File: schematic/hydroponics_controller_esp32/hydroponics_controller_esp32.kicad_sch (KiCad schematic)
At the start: 26 parts, among them J1 12v -, J10 RJ45, J11 5v-16v in, J12 12v_4_Channel_Relay, J13 Conn_01x04_Pin, J14 Conn_01x04_Pin, J2 12v +, J3 RJ45, J4 Power Input, J5 Flow Meters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

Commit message: Created Schematic PDF
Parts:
- added U9: 0-5v, symbol Amazon_Modules:Pressure Sensor
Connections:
- net at U6. (Blk): now also U5. (Blk); no longer U2. (GND)
- net at U8. (Blk): now also U7. (Blk); no longer U6. (Blk)
- net at U5. (Blk): now also U7. (Blk); no longer U6. (Blk)
- net at J12.2 (GND): now also J2.5 (Pin_5); no longer J14.GND
- net at J12.3 (IN1): now also U3.6 (D32_GPIO32)
- net at J12.6 (IN4): now also U3.10 (D27_GPIO27)
- net at J13.3v3: now also J10.1 (3v3), J4.3V3
- net at U2. (GND): now also U5. (Blk)
- net at J8.8 (A1): now also U9.3 (Vout)
- new net: U2. (GND), U6. (Blk)
- new net: U6. (Blk), U8. (Blk)
- new net: J12.1 (VCC), J13.5v, J8.1 (VCC), U4. (SIG), U9.2 (Vcc)
- new net: J12.2 (GND), J14.GND, U9.1 (GND)
- new net: U2. (GND), U7. (Blk)
- new net: U2. (GND), U8. (Blk)
- now unconnected: J13.5v, U4. (SIG)
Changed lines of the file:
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@@
 	)
 	(junction
+		(at 115.57 77.47)
+		(diameter 0)
+		(color 0 0 0 0)
+	)
+	(junction
 		(at 95.25 151.13)
 		(diameter 0)
@@
 	)
 	(junction
+		(at 101.6 72.39)
+		(diameter 0)
+		(color 0 0 0 0)
+	)
+	(junction
 		(at 231.14 156.21)
 		(diameter 0)
@@
 	(wire
 		(pts
-			(xy 101.6 77.47) (xy 101.6 58.42)
+			(xy 101.6 77.47) (xy 101.6 72.39)
+		)
+		(stroke
+			(width 0)
+			(type default)
+		)
+	)
+	(wire
+		(pts
+			(xy 106.68 74.93) (xy 106.68 72.39)
 		)
 		(stroke
@@
 	(wire
 		(pts
+			(xy 115.57 77.47) (xy 115.57 55.88)
+		)
+		(stroke
+			(width 0)
+			(type default)
+		)
+	)
+	(wire
+		(pts
+			(xy 196.85 85.09) (xy 196.85 100.33)
+		)
+		(stroke
+			(width 0)
+			(type default)
+		)
+	)
+	(wire
+		(pts
 			(xy 50.8 97.79) (xy 25.4 97.79)
 		)
@@
 	(wire
 		(pts
+			(xy 189.23 74.93) (xy 106.68 74.93)
+		)
+		(stroke
+			(width 0)
+			(type default)
+		)
+	)
+	(wire
+		(pts
 			(xy 45.72 165.1) (xy 45.72 148.59)
 		)
@@
 	(wire
 		(pts
+			(xy 210.82 74.93) (xy 210.82 87.63)
+		)
+		(stroke
+			(width 0)
+			(type default)
+		)
+	)
+	(wire
+		(pts
 			(xy 43.18 179.07) (xy 22.86 179.07)
 		)
@@
 	(wire
 		(pts
+			(xy 101.6 72.39) (xy 101.6 58.42)
+		)
+		(stroke
+			(width 0)
+			(type default)
+		)
+	)
+	(wire
+		(pts
+			(xy 106.68 72.39) (xy 101.6 72.39)
+		)
+		(stroke
+			(width 0)
+			(type default)
+		)
+	)
+	(wire
+		(pts
 			(xy 220.98 153.67) (xy 220.98 156.21)
 		)
@@
 	(wire
 		(pts
+			(xy 138.43 96.52) (xy 138.43 100.33)
+		)
+		(stroke
+			(width 0)
+			(type default)
+		)
+	)
+	(wire
+		(pts
 			(xy 128.27 107.95) (xy 128.27 101.6)
 		)
@@
 	(wire
 		(pts
+			(xy 210.82 87.63) (xy 154.94 87.63)
+		)
+		(stroke
+			(width 0)
+			(type default)
+		)
+	)
+	(wire
+		(pts
 			(xy 220.98 143.51) (xy 220.98 146.05)
 		)
@@
 	(wire
 		(pts
+			(xy 154.94 77.47) (xy 115.57 77.47)
+		)
+		(stroke
+			(width 0)
+			(type default)
+		)
+	)
+	(wire
+		(pts
 			(xy 233.68 73.66) (xy 238.76 73.66)
 		)
@@
 	(wire
 		(pts
-			(xy 115.57 99.06) (xy 115.57 55.88)
+			(xy 115.57 99.06) (xy 115.57 77.47)
 		)
 		(stroke
@@
 	(wire
 		(pts
+			(xy 154.94 87.63) (xy 154.94 77.47)
+		)
+		(stroke
+			(width 0)
+			(type default)
+		)
+	)
+	(wire
+		(pts
 			(xy 80.01 33.02) (xy 116.84 33.02)
 		)
@@
 	(wire
 		(pts
+			(xy 204.47 74.93) (xy 210.82 74.93)
+		)
+		(stroke
+			(width 0)
+			(type default)
+		)
+	)
+	(wire
+		(pts
 			(xy 209.55 121.92) (xy 209.55 143.51)
 		)
@@
 	(wire
 		(pts
+			(xy 196.85 100.33) (xy 138.43 100.33)
+		)
+		(stroke
+			(width 0)
+			(type default)
+		)
+	)
+	(wire
+		(pts
 			(xy 40.64 113.03) (xy 50.8 113.03)
 		)
@@
 					(unit 1)
 				)
+			)
+		)
+	)
+	(symbol
+		(lib_id "Amazon_Modules:Pressure Sensor")
+		(at 196.85 72.39 0)
+		(unit 1)
+		(exclude_from_sim no)
+		(in_bom yes)
+		(on_board yes)
+		(dnp no)
+		(fields_autoplaced yes)
+		(property "Reference" "U9"
+			(at 196.85 58.42 0)
+			(effects
+				(font
+					(size 1.27 1.27)
+				)
+			)
+		)
+		(property "Value" "0-5v"
+			(at 196.85 60.96 0)
+			(effects
+				(font
+					(size 1.27 1.27)
+				)
+			)
+		)
+		(property "Footprint" ""
+			(at 184.15 81.28 0)
+			(effects
+				(font
+					(size 1.27 1.27)
+				)
+				(hide yes)
+			)
+		)
+		(property "Datasheet" "https://www.amazon.com/dp/B0CSWFWCVK?ref=fed_asin_title&th=1"
+			(at 196.85 57.15 0)
+			(effects
+				(font
+					(size 1.27 1.27)
+				)
+				(hide yes)
+			)
+		)
+		(property "Description" "Submersible Liquid Level Sensor"
+			(at 196.088 92.202 0)
+			(effects
+				(font
+					(size 1.27 1.27)
+				)
+				(hide yes)
+			)
+		)
+		(pin "3"
+		)
+		(pin "1"
+		)
+		(pin "2"
+		)
+		(instances
+			(project ""
+				(path "/0e72da9f-540e-48b3-a96e-9cdd4d439927"
+					(reference "U9")
+					(unit 1)
+				)

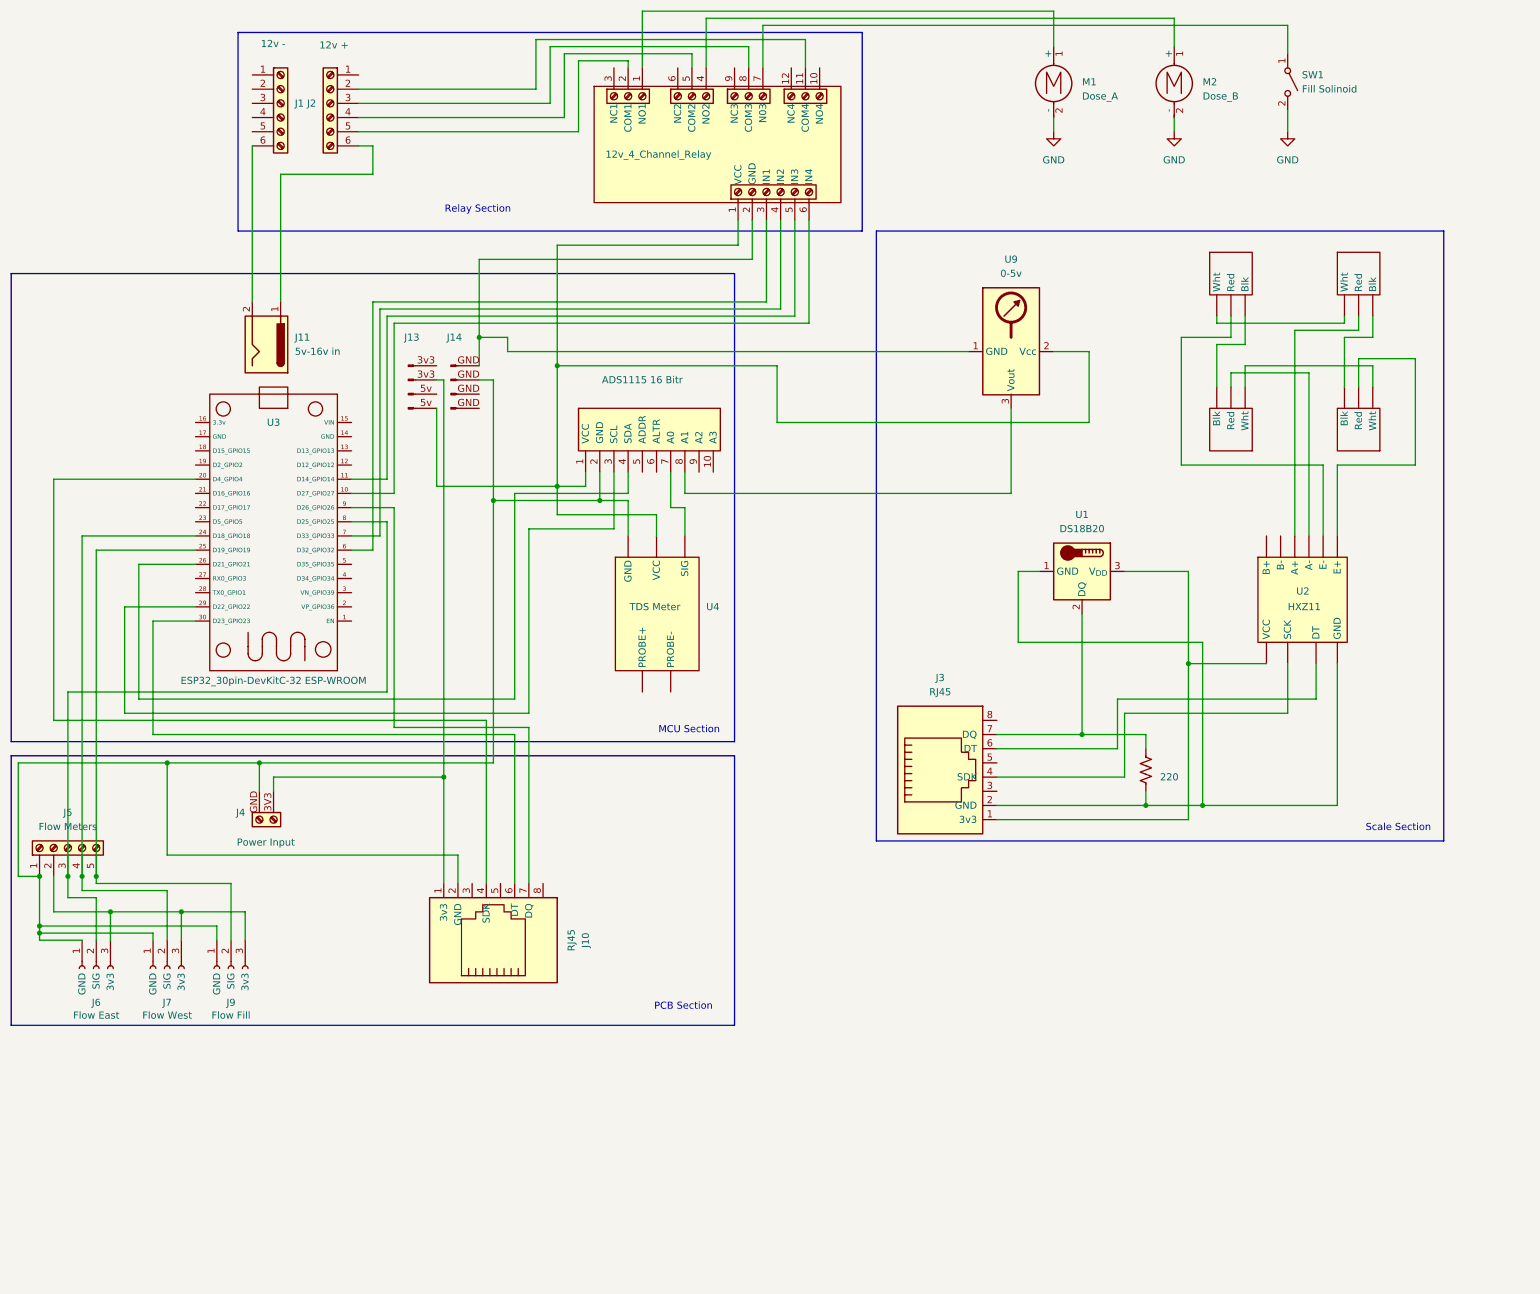
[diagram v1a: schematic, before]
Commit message: Hydroponics project architecture redesign
- Reorganized Home Assistant packages
- Added Node-RED workflow exports
- Added SQL schema
- Added engineering documentation
- Added project design documents
- Updated ESPHome controller
- Updated KiCad schematic
- Replaced nutrient mixing documentation
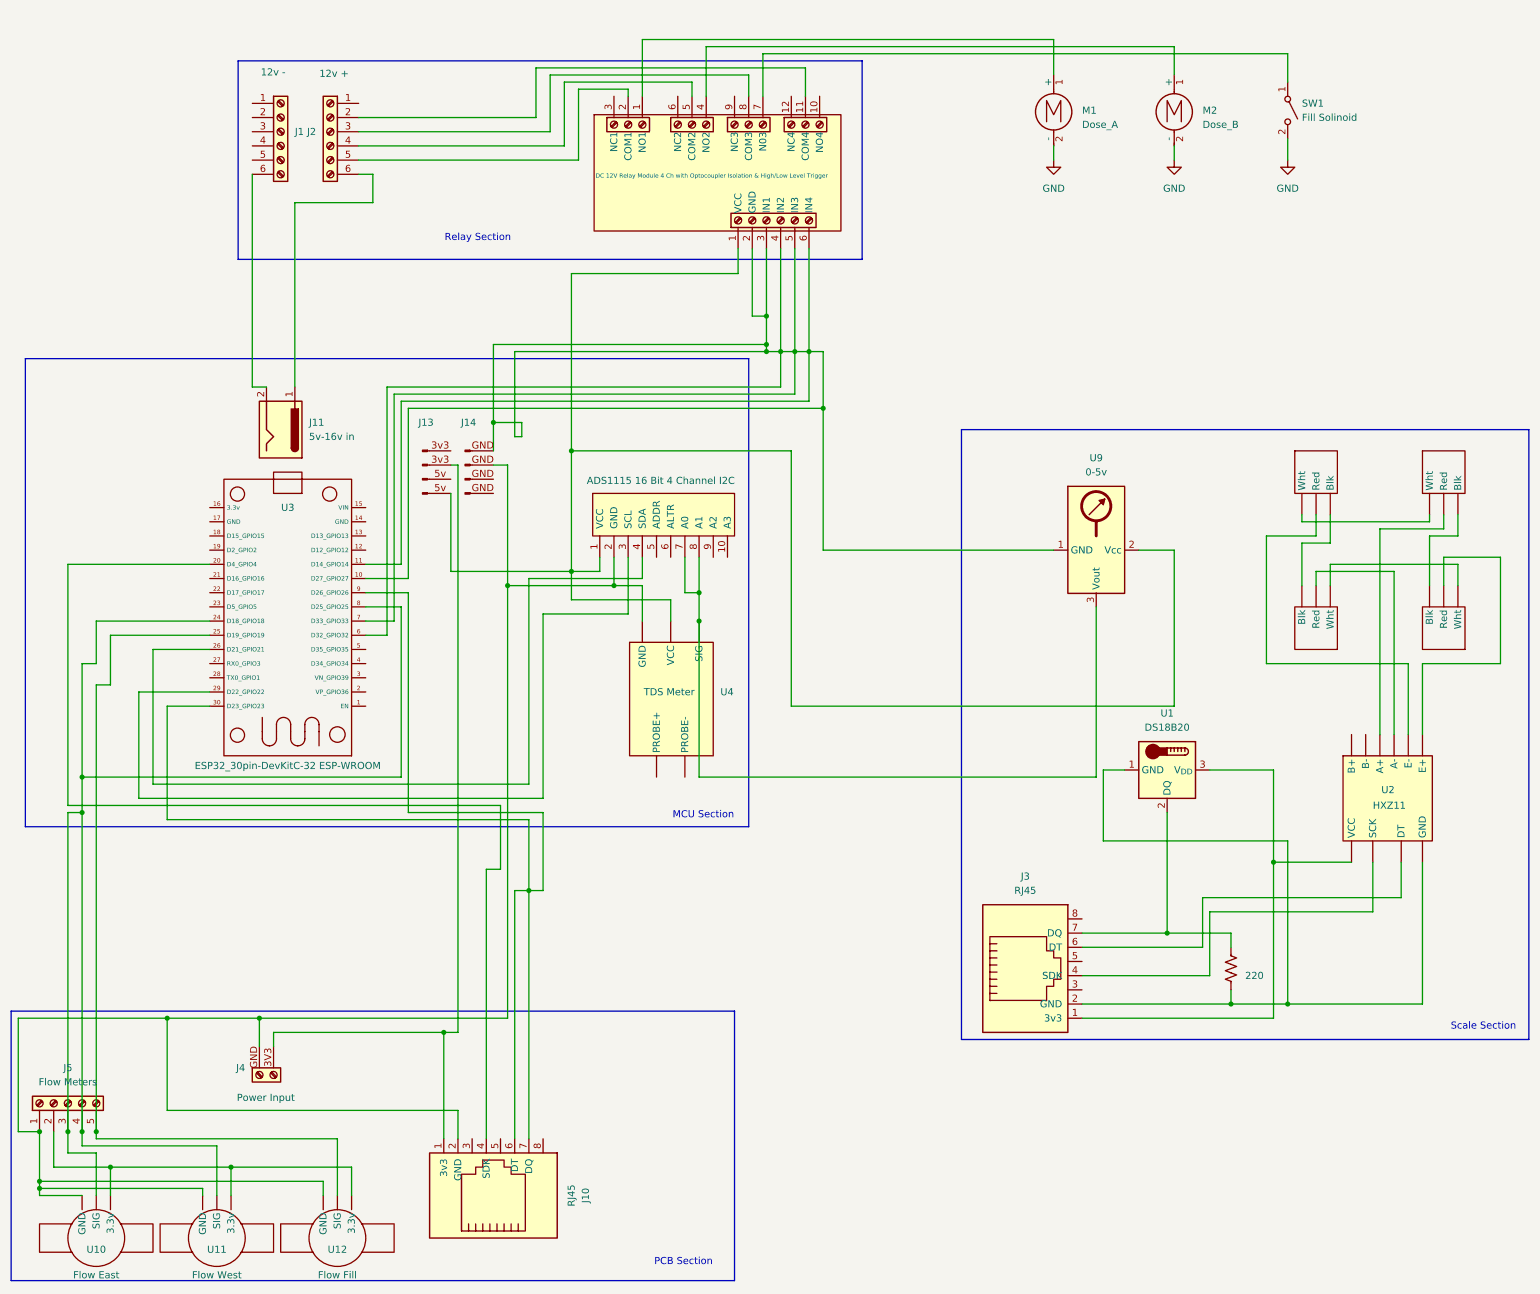
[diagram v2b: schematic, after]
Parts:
- removed J6: Flow East, symbol Connector:Conn_01x03_Socket
- removed J7: Flow West, symbol Connector:Conn_01x03_Socket
- removed J9: Flow Fill, symbol Connector:Conn_01x03_Socket
- added U10: Flow East, symbol Amazon_Modules:Flow_Meter-1/2{dblquote}
- added U11: Flow West, symbol Amazon_Modules:Flow_Meter-1/2{dblquote}
- added U12: Flow Fill, symbol Amazon_Modules:Flow_Meter-1/2{dblquote}
- J12: value 12v_4_Channel_Relay -> DC 12V Relay Module 4 Ch with Optocoupler Isolation & High/Low Level Trigger
- J8: value ADS1115 16 Bitr -> ADS1115 16 Bit 4 Channel I2C
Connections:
- net at U6. (Blk): now also U5. (Blk); no longer U2. (GND)
- net at U8. (Blk): now also U7. (Blk); no longer U6. (Blk)
- net at U5. (Blk): now also U7. (Blk); no longer U6. (Blk)
- net at J10.2 (GND), J14.GND, J4.GND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: now also U10. (3.3v), U11. (3.3v), U12. (3.3v)
- net at J5.2 (Pin_2): now also U10. (3.3v), U11. (3.3v), U12. (3.3v)
- net at J5.3 (Pin_3), U3.8 (D25_GPIO25): now also J5.4 (Pin_4), U3.24 (D18_GPIO18), U10. (3.3v), U11. (3.3v)
- net at J5.5 (Pin_5), U3.25 (D19_GPIO19): now also U12. (3.3v)
- net at J12.3 (IN1), U3.6 (D32_GPIO32): now also J12.2 (GND), J12.4 (IN2), J12.5 (IN3), J12.6 (IN4), J14.GND, U3.10 (D27_GPIO27), U3.11 (D14_GPIO14), U3.7 (D33_GPIO33), U9.1 (GND)
- net at J12.5 (IN3): now also J2.4 (Pin_4); no longer U3.11 (D14_GPIO14)
- net at J13.3v3: now also J10.1 (3v3), J4.3V3
- net at U2. (GND): now also U5. (Blk)
- net at J8.7 (A0), U4. (SIG): now also J8.8 (A1), U9.3 (Vout)
- net at J10.6 (DT), U3.30 (D23_GPIO23): now also J10.7 (DQ), U3.9 (D26_GPIO26)
- new net: U2. (GND), U6. (Blk)
- new net: U6. (Blk), U8. (Blk)
- new net: J12.1 (VCC), J13.5v, J8.1 (VCC), U4. (SIG), U9.2 (Vcc)
- new net: U2. (GND), U7. (Blk)
- new net: U2. (GND), U8. (Blk)
- now unconnected: J12.6 (IN4), J13.5v, J14.GND, U4. (SIG)
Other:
- moved on the sheet: J1, J10, J11, J13, J14, J2, J3, J4, J5, M1, M2, SW1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
